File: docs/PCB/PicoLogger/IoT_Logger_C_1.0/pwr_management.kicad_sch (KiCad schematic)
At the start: 13 parts, among them U3 AP63200WU

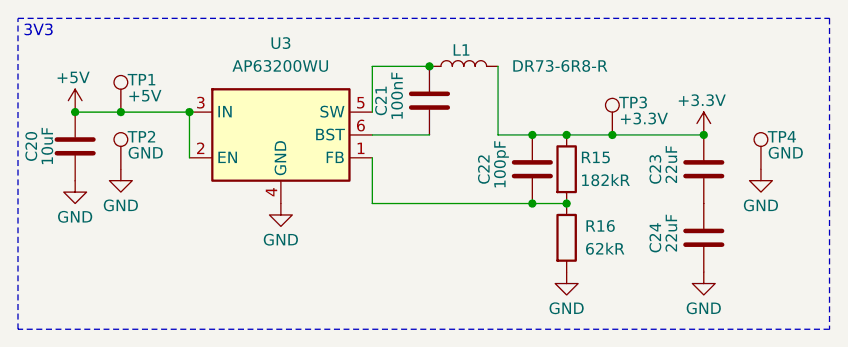
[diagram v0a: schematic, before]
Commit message: Logger IoT B and C production files generated, backend and frontend prepared for new logger type.
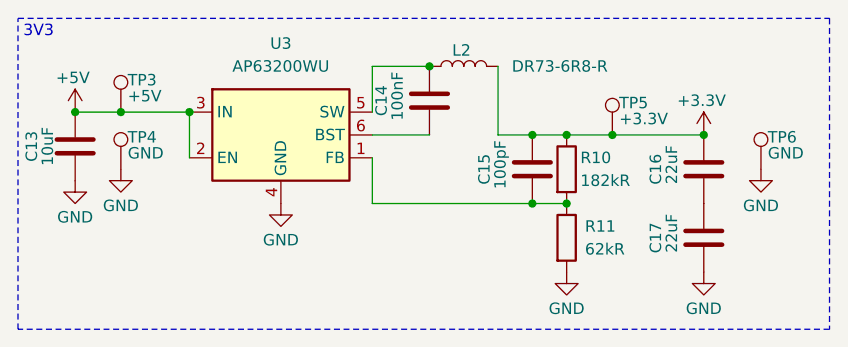
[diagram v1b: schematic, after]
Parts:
- renumbered C20 to C13, C21 to C14, C22 to C15, C23 to C16, C24 to C17, L1 to L2, R15 to R10, R16 to R11, TP1 to TP3, TP2 to TP4, TP3 to TP5, TP4 to TP6
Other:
- title: IoT Logger A - Power Management -> IoT Logger C - Power Management
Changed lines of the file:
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@@
 	(paper "A4")
 	(title_block
-		(title "IoT Logger A - Power Management")
+		(title "IoT Logger C - Power Management")
 		(date "2026-01-24")
 		(rev "1.0")
@@
 		(on_board yes)
 		(dnp no)
-		(property "Reference" "#PWR040"
+		(property "Reference" "#PWR030"
 			(at 139.7 100.33 0)
 			(effects
@@
 			(project "PicoLogger_Small"
 				(path "/2910198d-e123-424f-9561-5234a772fa41/8f2aecdf-3fb8-476b-9b06-dcd68d3e68d4"
-					(reference "#PWR040")
+					(reference "#PWR030")
 					(unit 1)
 				)
@@
 		(on_board yes)
 		(dnp no)
-		(property "Reference" "TP2"
+		(property "Reference" "TP4"
 			(at 122.682 86.614 0)
 			(effects
@@
 			(project "IoT_Logger_A_1.0"
 				(path "/2910198d-e123-424f-9561-5234a772fa41/8f2aecdf-3fb8-476b-9b06-dcd68d3e68d4"
-					(reference "TP2")
+					(reference "TP4")
 					(unit 1)
 				)
@@
 		(on_board yes)
 		(dnp no)
-		(property "Reference" "L1"
+		(property "Reference" "L2"
 			(at 159.766 76.962 90)
 			(effects
@@
 			(project "PicoLogger_Small"
 				(path "/2910198d-e123-424f-9561-5234a772fa41/8f2aecdf-3fb8-476b-9b06-dcd68d3e68d4"
-					(reference "L1")
+					(reference "L2")
 					(unit 1)
 				)
@@
 		(on_board yes)
 		(dnp no)
-		(property "Reference" "C23"
+		(property "Reference" "C16"
 			(at 181.356 90.17 90)
 			(effects
@@
 			(project "PicoLogger_Small"
 				(path "/2910198d-e123-424f-9561-5234a772fa41/8f2aecdf-3fb8-476b-9b06-dcd68d3e68d4"
-					(reference "C23")
+					(reference "C16")
 					(unit 1)
 				)
@@
 		(on_board yes)
 		(dnp no)
-		(property "Reference" "#PWR038"
+		(property "Reference" "#PWR027"
 			(at 116.84 87.63 0)
 			(effects
@@
 			(project "PicoLogger_Small"
 				(path "/2910198d-e123-424f-9561-5234a772fa41/8f2aecdf-3fb8-476b-9b06-dcd68d3e68d4"
-					(reference "#PWR038")
+					(reference "#PWR027")
 					(unit 1)
 				)
@@
 		(on_board yes)
 		(dnp no)
-		(property "Reference" "R15"
+		(property "Reference" "R10"
 			(at 172.974 88.9 0)
 			(effects
@@
 			(project "PicoLogger_Small"
 				(path "/2910198d-e123-424f-9561-5234a772fa41/8f2aecdf-3fb8-476b-9b06-dcd68d3e68d4"
-					(reference "R15")
+					(reference "R10")
 					(unit 1)
 				)
@@
 		(on_board yes)
 		(dnp no)
-		(property "Reference" "TP4"
+		(property "Reference" "TP6"
 			(at 193.802 86.614 0)
 			(effects
@@
 			(project "IoT_Logger_A_1.0"
 				(path "/2910198d-e123-424f-9561-5234a772fa41/8f2aecdf-3fb8-476b-9b06-dcd68d3e68d4"
-					(reference "TP4")
+					(reference "TP6")
 					(unit 1)
 				)
@@
 		(on_board yes)
 		(dnp no)
-		(property "Reference" "#PWR091"
+		(property "Reference" "#PWR034"
 			(at 193.04 96.52 0)
 			(effects
@@
 			(project "IoT_Logger_A_1.0"
 				(path "/2910198d-e123-424f-9561-5234a772fa41/8f2aecdf-3fb8-476b-9b06-dcd68d3e68d4"
-					(reference "#PWR091")
+					(reference "#PWR034")
 					(unit 1)
 				)
@@
 		(on_board yes)
 		(dnp no)
-		(property "Reference" "#PWR090"
+		(property "Reference" "#PWR029"
 			(at 121.92 96.52 0)
 			(effects
@@
 			(project "IoT_Logger_A_1.0"
 				(path "/2910198d-e123-424f-9561-5234a772fa41/8f2aecdf-3fb8-476b-9b06-dcd68d3e68d4"
-					(reference "#PWR090")
+					(reference "#PWR029")
 					(unit 1)
 				)
@@
 		(on_board yes)
 		(dnp no)
-		(property "Reference" "C24"
+		(property "Reference" "C17"
 			(at 181.356 97.79 90)
 			(effects
@@
 			(project "PicoLogger_Small"
 				(path "/2910198d-e123-424f-9561-5234a772fa41/8f2aecdf-3fb8-476b-9b06-dcd68d3e68d4"
-					(reference "C24")
+					(reference "C17")
 					(unit 1)
 				)
@@
 		(on_board yes)
 		(dnp no)
-		(property "Reference" "TP1"
+		(property "Reference" "TP3"
 			(at 122.682 80.264 0)
 			(effects
@@
 			(project ""
 				(path "/2910198d-e123-424f-9561-5234a772fa41/8f2aecdf-3fb8-476b-9b06-dcd68d3e68d4"
-					(reference "TP1")
+					(reference "TP3")
 					(unit 1)
 				)
@@
 		(on_board yes)
 		(dnp no)
-		(property "Reference" "TP3"
+		(property "Reference" "TP5"
 			(at 177.292 82.804 0)
 			(effects
@@
 			(project "IoT_Logger_A_1.0"
 				(path "/2910198d-e123-424f-9561-5234a772fa41/8f2aecdf-3fb8-476b-9b06-dcd68d3e68d4"
-					(reference "TP3")
+					(reference "TP5")
 					(unit 1)
 				)
@@
 		(on_board yes)
 		(dnp no)
-		(property "Reference" "C21"
+		(property "Reference" "C14"
 			(at 150.876 82.55 90)
 			(effects
@@
 			(project "PicoLogger_Small"
 				(path "/2910198d-e123-424f-9561-5234a772fa41/8f2aecdf-3fb8-476b-9b06-dcd68d3e68d4"
-					(reference "C21")
+					(reference "C14")
 					(unit 1)
 				)
@@
 		(on_board yes)
 		(dnp no)
-		(property "Reference" "#PWR042"
+		(property "Reference" "#PWR032"
 			(at 186.69 90.17 0)
 			(effects
@@
 			(project "PicoLogger_Small"
 				(path "/2910198d-e123-424f-9561-5234a772fa41/8f2aecdf-3fb8-476b-9b06-dcd68d3e68d4"
-					(reference "#PWR042")
+					(reference "#PWR032")
 					(unit 1)
 				)
@@
 		(on_board yes)
 		(dnp no)
-		(property "Reference" "C20"
+		(property "Reference" "C13"
 			(at 112.014 87.63 90)
 			(effects
@@
 			(project "PicoLogger_Small"
 				(path "/2910198d-e123-424f-9561-5234a772fa41/8f2aecdf-3fb8-476b-9b06-dcd68d3e68d4"
-					(reference "C20")
+					(reference "C13")
 					(unit 1)
 				)
@@
 		(on_board yes)
 		(dnp no)
-		(property "Reference" "R16"
+		(property "Reference" "R11"
 			(at 173.482 96.52 0)
 			(effects
@@
 			(project "PicoLogger_Small"
 				(path "/2910198d-e123-424f-9561-5234a772fa41/8f2aecdf-3fb8-476b-9b06-dcd68d3e68d4"
-					(reference "R16")
+					(reference "R11")
 					(unit 1)
 				)
@@
 		(on_board yes)
 		(dnp no)
-		(property "Reference" "#PWR043"
+		(property "Reference" "#PWR033"
 			(at 186.69 107.95 0)
 			(effects
@@
 			(project "PicoLogger_Small"
 				(path "/2910198d-e123-424f-9561-5234a772fa41/8f2aecdf-3fb8-476b-9b06-dcd68d3e68d4"
-					(reference "#PWR043")
+					(reference "#PWR033")
 					(unit 1)
 				)
@@
 		(on_board yes)
 		(dnp no)
-		(property "Reference" "#PWR041"
+		(property "Reference" "#PWR031"
 			(at 171.45 107.95 0)
 			(effects
@@
 			(project "PicoLogger_Small"
 				(path "/2910198d-e123-424f-9561-5234a772fa41/8f2aecdf-3fb8-476b-9b06-dcd68d3e68d4"
-					(reference "#PWR041")
+					(reference "#PWR031")
 					(unit 1)
 				)
@@
 		(on_board yes)
 		(dnp no)
-		(property "Reference" "C22"
+		(property "Reference" "C15"
 			(at 162.306 90.17 90)
 			(effects
@@
 			(project "PicoLogger_Small"
 				(path "/2910198d-e123-424f-9561-5234a772fa41/8f2aecdf-3fb8-476b-9b06-dcd68d3e68d4"
-					(reference "C22")
+					(reference "C15")
 					(unit 1)
 				)
@@
 		(on_board yes)
 		(dnp no)
-		(property "Reference" "#PWR039"
+		(property "Reference" "#PWR028"
 			(at 116.84 97.79 0)
 			(effects
@@
 			(project "PicoLogger_Small"
 				(path "/2910198d-e123-424f-9561-5234a772fa41/8f2aecdf-3fb8-476b-9b06-dcd68d3e68d4"
-					(reference "#PWR039")
-					(unit 1)
-				)
+					(reference "#PWR028")
+					(unit 1)
+				)
